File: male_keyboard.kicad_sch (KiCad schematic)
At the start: 40 parts, among them J1 Elite-Pi Microcontroller, J2 AudioJack4, J3 AudioJack4, J4 Elite-Pi Microcontroller, SW1 SW_Push, SW10 SW_Push, SW11 SW_Push, SW12 SW_Push, SW13 SW_Push, SW14 SW_Push, SW15 SW_Push, SW16 SW_Push, SW17 SW_Push, SW18 SW_Push, SW19 SW_Push, SW2 SW_Push, SW20 SW_Push, SW21 SW_Push, SW22 SW_Push, SW23 SW_Push, SW24 SW_Push, SW25 SW_Push, SW26 SW_Push, SW27 SW_Push, SW28 SW_Push, SW29 SW_Push, SW3 SW_Push, SW30 SW_Push, SW31 SW_Push, SW32 SW_Push, SW33 SW_Push, SW34 SW_Push, SW35 SW_Push, SW36 SW_Push, SW4 SW_Push, SW6 SW_Push, SW7 SW_Push, SW8 SW_Push, SW9 SW_Push

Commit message: merge and some more updates
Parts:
- renumbered SW15 to SW10, SW18 to SW15, SW19 to SW18, SW10 to SW5
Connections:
- net 10: no longer J1.25 (Pin_25)
- net 11: now also J1.25 (Pin_25); no longer J1.26 (Pin_26)
- net 12: now also J1.26 (Pin_26); no longer J1.27 (Pin_27)
- net 13: now also J1.27 (Pin_27); no longer J1.28 (Pin_28)
- net 14: now also J1.28 (Pin_28); no longer J1.29 (Pin_29)
- net 15: now also J1.29 (Pin_29); no longer J1.13 (Pin_13)
- net 16: now also J1.13 (Pin_13); no longer J1.14 (Pin_14)
- net 17: now also J1.14 (Pin_14); no longer J1.15 (Pin_15)
- net 18: now also J1.15 (Pin_15); no longer J1.16 (Pin_16)
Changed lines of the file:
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@@
 	(wire
 		(pts
-			(xy 69.85 106.68) (xy 81.28 106.68)
-		)
-		(stroke
-			(width 0)
-			(type default)
-		)
-	)
-	(wire
-		(pts
 			(xy 232.41 120.65) (xy 232.41 125.73)
 		)
@@
 		)
 	)
-	(global_label "18"
-		(shape input)
-		(at 81.28 106.68 0)
-		(fields_autoplaced yes)
-		(effects
-			(font
-				(size 1.27 1.27)
-			)
-			(justify left)
-		)
-		(property "Intersheetrefs" "${INTERSHEET_REFS}"
-			(at 86.6842 106.68 0)
-			(effects
-				(font
-					(size 1.27 1.27)
-				)
-				(justify left)
-				(hide yes)
-			)
-		)
-	)
 	(global_label "9"
 		(shape input)
@@
 		)
 	)
-	(global_label "17"
+	(global_label "18"
 		(shape input)
 		(at 81.28 109.22 0)
@@
 		)
 	)
-	(global_label "13"
+	(global_label "14"
 		(shape input)
 		(at 60.96 124.46 270)
@@
 		)
 	)
-	(global_label "14"
+	(global_label "15"
 		(shape input)
 		(at 63.5 124.46 270)
@@
 		)
 	)
-	(global_label "16"
+	(global_label "17"
 		(shape input)
 		(at 81.28 111.76 0)
@@
 		)
 	)
-	(global_label "12"
+	(global_label "13"
 		(shape input)
 		(at 58.42 124.46 270)
@@
 		)
 	)
-	(global_label "15"
+	(global_label "16"
 		(shape input)
 		(at 81.28 114.3 0)
@@
 		)
 	)
-	(global_label "10"
+	(global_label "11"
 		(shape input)
 		(at 53.34 124.46 270)
@@
 		)
 	)
-	(global_label "11"
+	(global_label "12"
 		(shape input)
 		(at 55.88 124.46 270)
@@
 		(dnp no)
 		(fields_autoplaced yes)
-		(property "Reference" "SW19"
+		(property "Reference" "SW18"
 			(at 95.25 57.15 0)
 			(effects
@@
 			(project "male_keyboard"
 				(path "/58898b31-0272-4fd0-b6ca-dcb6784775e4"
-					(reference "SW19")
+					(reference "SW18")
 					(unit 1)
 				)
@@
 		(dnp no)
 		(fields_autoplaced yes)
-		(property "Reference" "SW18"
+		(property "Reference" "SW15"
 			(at 95.25 44.45 0)
 			(effects
@@
 			(project "male_keyboard"
 				(path "/58898b31-0272-4fd0-b6ca-dcb6784775e4"
-					(reference "SW18")
+					(reference "SW15")
 					(unit 1)
 				)
@@
 		(dnp no)
 		(fields_autoplaced yes)
-		(property "Reference" "SW10"
+		(property "Reference" "SW5"
 			(at 95.25 19.05 0)
 			(effects
@@
 			(project "male_keyboard"
 				(path "/58898b31-0272-4fd0-b6ca-dcb6784775e4"
-					(reference "SW10")
+					(reference "SW5")
 					(unit 1)
 				)
@@
 		(dnp no)
 		(fields_autoplaced yes)
-		(property "Reference" "SW15"
+		(property "Reference" "SW10"
 			(at 95.25 31.75 0)
 			(effects
@@
 			(project "male_keyboard"
 				(path "/58898b31-0272-4fd0-b6ca-dcb6784775e4"
-					(reference "SW15")
+					(reference "SW10")
 					(unit 1)
 				)

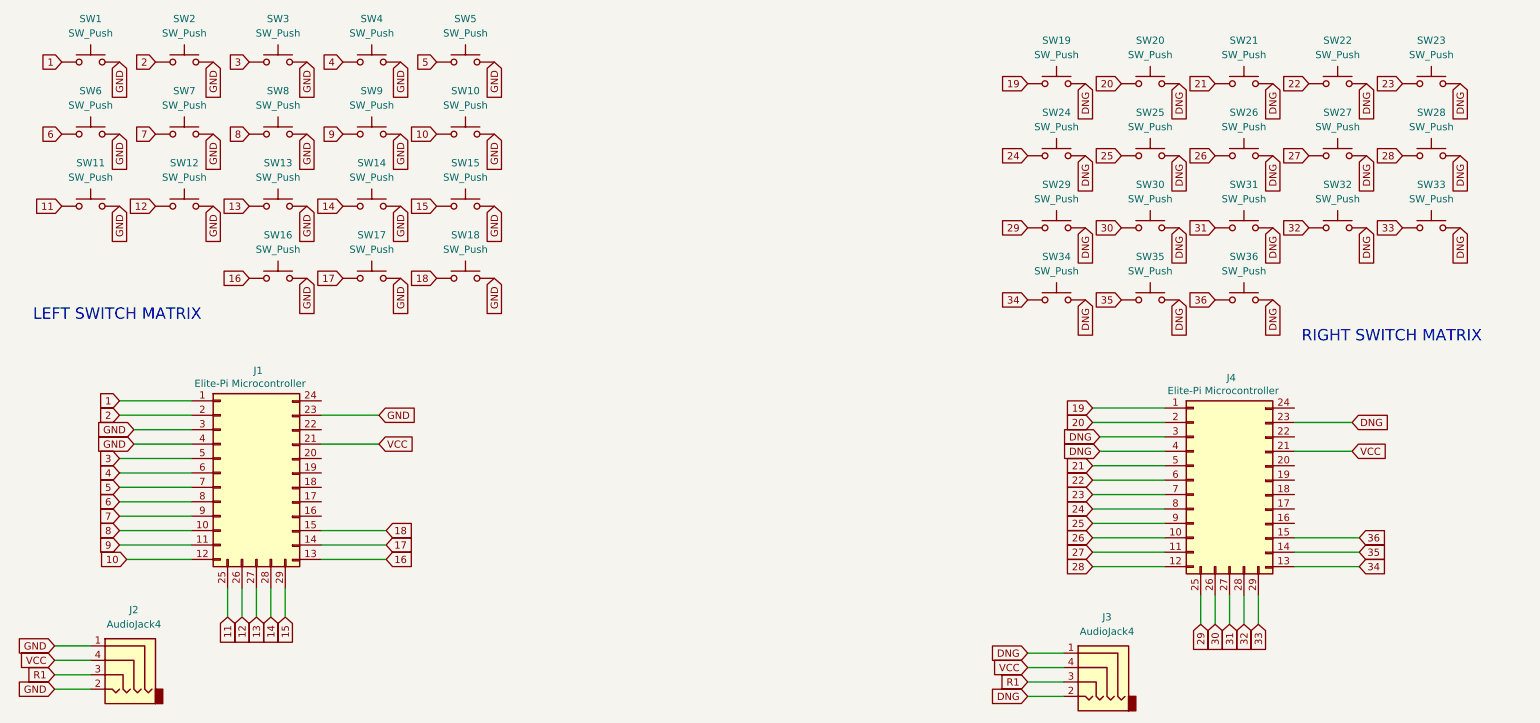
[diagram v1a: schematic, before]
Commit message: add ground plate and wires
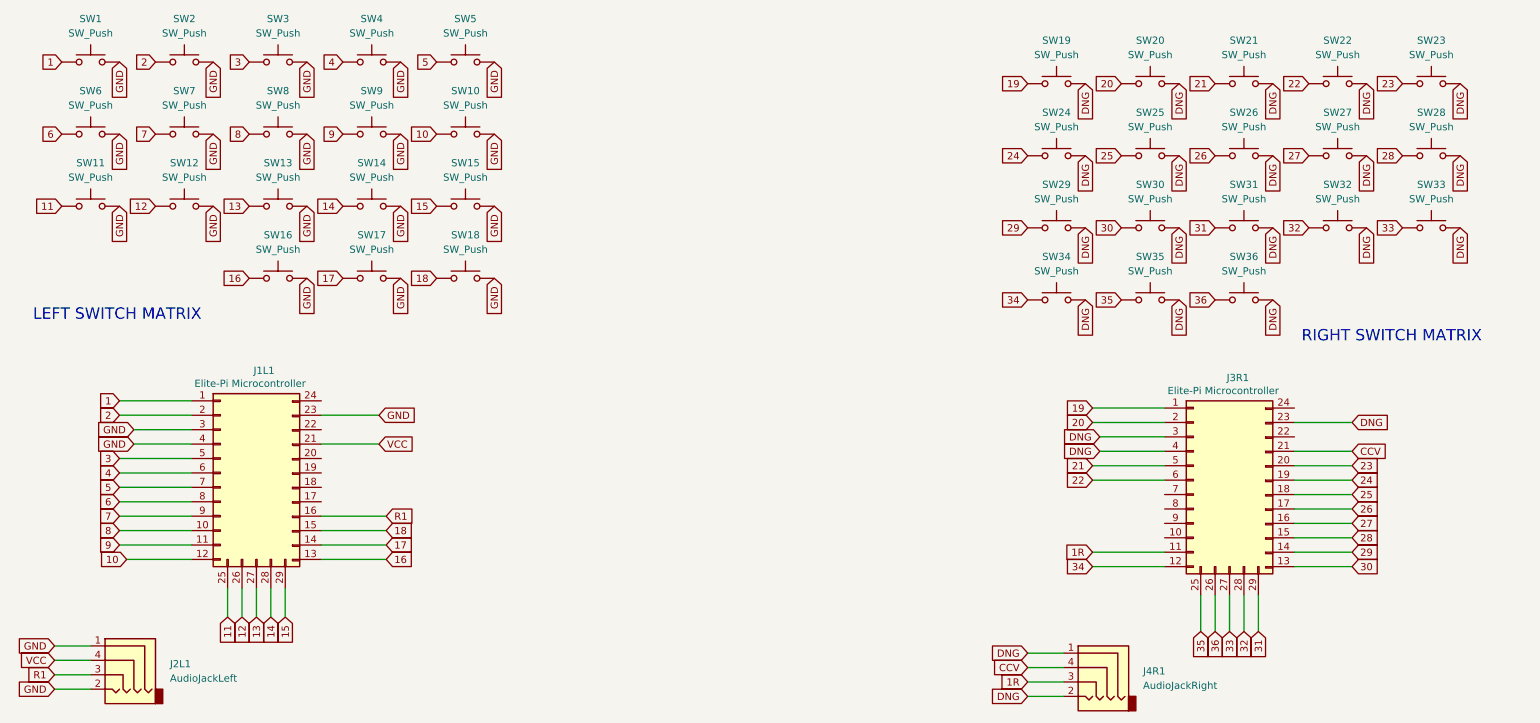
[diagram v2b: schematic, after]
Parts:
- J2L1: renamed from J2; value AudioJack4 -> AudioJackLeft
- J4R1: renamed from J3; value AudioJack4 -> AudioJackRight
- renumbered J1 to J1L1, J4 to J3R1
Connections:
- net 23: now also J3R1.20 (Pin_20); no longer J3R1.7 (Pin_7)
- net 24: now also J3R1.19 (Pin_19); no longer J3R1.8 (Pin_8)
- net 25: now also J3R1.18 (Pin_18); no longer J3R1.9 (Pin_9)
- net 26: now also J3R1.17 (Pin_17); no longer J3R1.10 (Pin_10)
- net 27: now also J3R1.16 (Pin_16); no longer J3R1.11 (Pin_11)
- net 28: now also J3R1.15 (Pin_15); no longer J3R1.12 (Pin_12)
- net 29: now also J3R1.14 (Pin_14); no longer J3R1.25 (Pin_25)
- net 30: now also J3R1.13 (Pin_13); no longer J3R1.26 (Pin_26)
- net 31: now also J3R1.29 (Pin_29); no longer J3R1.27 (Pin_27)
- net 33: now also J3R1.27 (Pin_27); no longer J3R1.29 (Pin_29)
- net 34: now also J3R1.12 (Pin_12); no longer J3R1.13 (Pin_13)
- net 35: now also J3R1.25 (Pin_25); no longer J3R1.14 (Pin_14)
- net 36: now also J3R1.26 (Pin_26); no longer J3R1.15 (Pin_15)
- net R1: now also J1L1.16 (Pin_16); no longer J4R1.3
- net VCC: no longer J3R1.21 (Pin_21), J4R1.4
- new net 1R: J3R1.11 (Pin_11), J4R1.3
- new net CCV: J3R1.21 (Pin_21), J4R1.4
